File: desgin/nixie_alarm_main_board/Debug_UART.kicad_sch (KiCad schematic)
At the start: 1 part, among them J4 JST XH 2.54 3 pin

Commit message: copper border
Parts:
- removed J4: JST XH 2.54 3 pin, Connector_JST:JST_EH_S2B-EH_1x02_P2.50mm_Horizontal, symbol Connector:Conn_01x02_Pin
- added J5: Goldpin 3pin, Connector_PinHeader_2.54mm:PinHeader_1x03_P2.54mm_Horizontal, symbol Connector:Conn_01x03_Pin
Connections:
- net DEBUG_UART_RX: now also J5.2 (Pin_2)
- net DEBUG_UART_TX: now also J5.1 (Pin_1)
- new net GND: J5.3 (Pin_3)
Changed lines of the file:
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@@
 	(generator_version "8.0")
 	(paper "A4")
+	(wire
+		(pts
+			(xy 118.618 101.854) (xy 118.618 103.378)
+		)
+		(stroke
+			(width 0)
+			(type default)
+		)
+	)
 	(global_label "DEBUG_UART_RX"
 		(shape input)
-		(at 130.556 93.218 0)
+		(at 118.618 99.314 0)
 		(fields_autoplaced yes)
 		(effects
@@
 		)
 		(property "Intersheetrefs" "${INTERSHEET_REFS}"
-			(at 148.9021 93.218 0)
+			(at 136.9641 99.314 0)
 			(effects
 				(font
@@
 	(global_label "DEBUG_UART_TX"
 		(shape input)
-		(at 130.556 90.678 0)
+		(at 118.618 96.774 0)
 		(fields_autoplaced yes)
 		(effects
@@
 		)
 		(property "Intersheetrefs" "${INTERSHEET_REFS}"
-			(at 148.5997 90.678 0)
+			(at 136.6617 96.774 0)
 			(effects
 				(font
@@
 	)
 	(symbol
-		(lib_id "Connector:Conn_01x02_Pin")
-		(at 125.476 90.678 0)
+		(lib_id "power:GND")
+		(at 118.618 103.378 0)
 		(unit 1)
 		(exclude_from_sim no)
@@
 		(dnp no)
 		(fields_autoplaced yes)
-		(property "Reference" "J4"
-			(at 126.111 85.09 0)
+		(property "Reference" "#PWR041"
+			(at 118.618 109.728 0)
+			(effects
+				(font
+					(size 1.27 1.27)
+				)
+				(hide yes)
+			)
+		)
+		(property "Value" "GND"
+			(at 118.618 108.458 0)
 			(effects
 				(font
@@
 			)
 		)
-		(property "Value" "JST XH 2.54 3 pin"
-			(at 126.111 87.63 0)
+		(property "Footprint" ""
+			(at 118.618 103.378 0)
+			(effects
+				(font
+					(size 1.27 1.27)
+				)
+				(hide yes)
+			)
+		)
+		(property "Datasheet" ""
+			(at 118.618 103.378 0)
+			(effects
+				(font
+					(size 1.27 1.27)
+				)
+				(hide yes)
+			)
+		)
+		(property "Description" "Power symbol creates a global label with name \"GND\" , ground"
+			(at 118.618 103.378 0)
+			(effects
+				(font
+					(size 1.27 1.27)
+				)
+				(hide yes)
+			)
+		)
+		(pin "1"
+		)
+		(instances
+			(project "nixie_alarm_main_board"
+				(path "/a0d555d7-39a0-4a98-b831-70d97d0aa5a1/1fdd9e0c-5909-450c-9e00-c17b847bc6ac"
+					(reference "#PWR041")
+					(unit 1)
+				)
+			)
+		)
+	)
+	(symbol
+		(lib_id "Connector:Conn_01x03_Pin")
+		(at 113.538 99.314 0)
+		(unit 1)
+		(exclude_from_sim no)
+		(in_bom yes)
+		(on_board yes)
+		(dnp no)
+		(property "Reference" "J5"
+			(at 116.332 91.44 0)
 			(effects
 				(font
@@
 			)
 		)
-		(property "Footprint" "Connector_JST:JST_EH_S2B-EH_1x02_P2.50mm_Horizontal"
-			(at 125.476 90.678 0)
+		(property "Value" "Goldpin 3pin "
+			(at 116.84 93.726 0)
+			(effects
+				(font
+					(size 1.27 1.27)
+				)
+			)
+		)
+		(property "Footprint" "Connector_PinHeader_2.54mm:PinHeader_1x03_P2.54mm_Horizontal"
+			(at 113.538 99.314 0)
 			(effects
 				(font
@@
 		)
 		(property "Datasheet" "~"
-			(at 125.476 90.678 0)
+			(at 113.538 99.314 0)
 			(effects
 				(font
@@
 			)
 		)
-		(property "Description" "Generic connector, single row, 01x02, script generated"
-			(at 125.476 90.678 0)
+		(property "Description" "Generic connector, single row, 01x03, script generated"
+			(at 113.538 99.314 0)
 			(effects
 				(font
@@
 		(pin "2"
 		)
+		(pin "3"
+		)
 		(pin "1"
 		)
@@
 			(project "nixie_alarm_main_board"
 				(path "/a0d555d7-39a0-4a98-b831-70d97d0aa5a1/1fdd9e0c-5909-450c-9e00-c17b847bc6ac"
-					(reference "J4")
+					(reference "J5")
 					(unit 1)
 				)

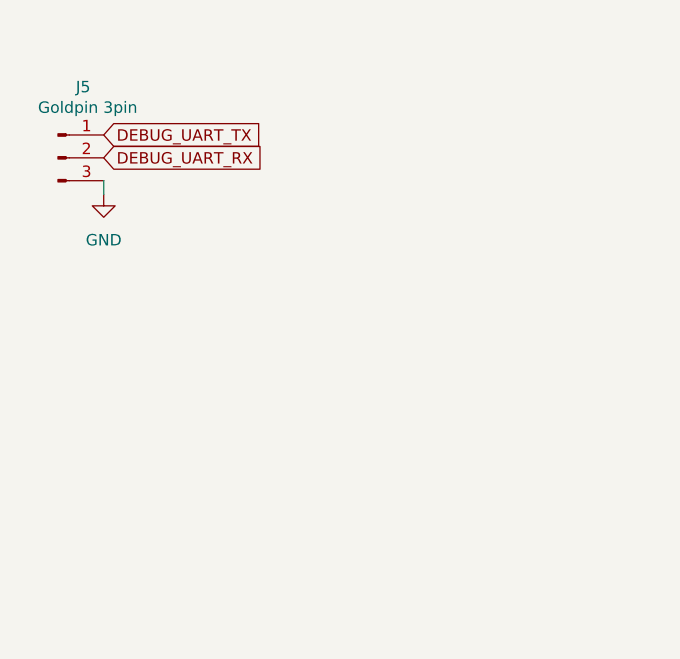
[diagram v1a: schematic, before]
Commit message: tvs added
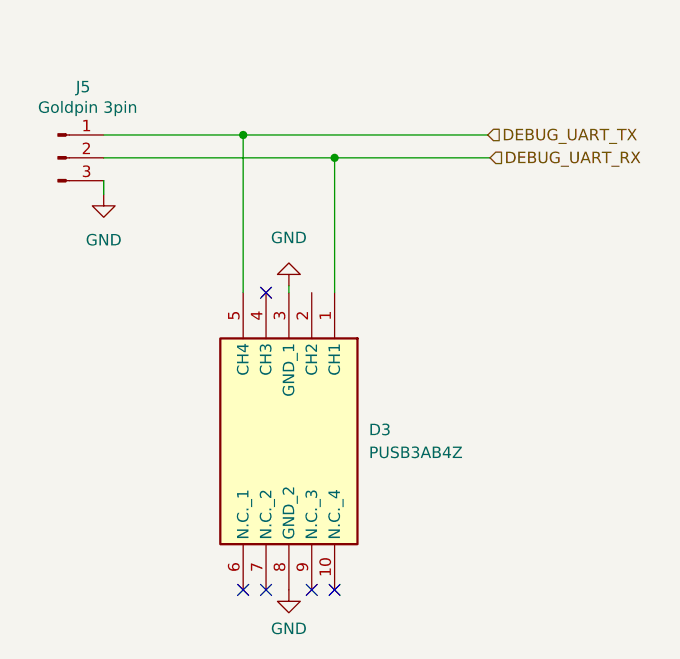
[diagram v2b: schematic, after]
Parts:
- added D3: PUSB3AB4Z, SON50P100X250X50-10N, symbol SamacSys_Parts:PUSB3AB4Z
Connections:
- net DEBUG_UART_RX: now also D3.1 (CH1)
- net DEBUG_UART_TX: now also D3.5 (CH4)
- net GND: now also D3.3 (GND_1), D3.8 (GND_2)
- no-connect marks 0 -> 5

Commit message: fixes added
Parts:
- J5: value Goldpin 3pin -> Goldpin 3pin
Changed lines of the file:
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@@
 			)
 		)
-		(property "Value" "Goldpin 3pin "
+		(property "Value" "Goldpin 3pin"
 			(at 116.84 93.726 0)
 			(effects
